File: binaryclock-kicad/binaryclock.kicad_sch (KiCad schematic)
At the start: 19 parts, among them J1 Conn_01x03_Pin, J2 AVR-ISP-6, SW1 SW_Push, SW2 SW_Push, SW3 SW_Push, U1 ATmega48-20P, Y1 Crystal

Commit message: assigned footprints to components
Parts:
- BT1: footprint (none) -> Battery:BatteryHolder_Keystone_103_1x20mm
- D1, D10, D11, D2, D3, D4, D5, D6, D7, D8, D9: footprint (none) -> LED_THT:LED_D3.0mm
- J1: footprint Connector_PinHeader_1.27mm:PinHeader_1x03_P1.27mm_Vertical -> Connector_PinHeader_2.54mm:PinHeader_1x03_P2.54mm_Vertical
- SW1, SW2, SW3: footprint (none) -> Button_Switch_THT:SW_PUSH_6mm
- Y1: footprint Crystal:Crystal_DS10_D1.0mm_L4.3mm_Vertical -> Crystal:Crystal_Round_D2.0mm_Vertical
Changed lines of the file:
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@@
 			)
 		)
-		(property "Footprint" ""
+		(property "Footprint" "LED_THT:LED_D3.0mm"
 			(at 140.97 76.2 0)
 			(effects
@@
 			)
 		)
-		(property "Footprint" "Connector_PinHeader_1.27mm:PinHeader_1x03_P1.27mm_Vertical"
+		(property "Footprint" "Connector_PinHeader_2.54mm:PinHeader_1x03_P2.54mm_Vertical"
 			(at 196.85 107.95 0)
 			(effects
@@
 			)
 		)
-		(property "Footprint" ""
+		(property "Footprint" "LED_THT:LED_D3.0mm"
 			(at 123.19 76.2 0)
 			(effects
@@
 			)
 		)
-		(property "Footprint" ""
+		(property "Footprint" "LED_THT:LED_D3.0mm"
 			(at 203.2 76.2 0)
 			(effects
@@
 			)
 		)
-		(property "Footprint" ""
+		(property "Footprint" "Button_Switch_THT:SW_PUSH_6mm"
 			(at 140.97 144.78 0)
 			(effects
@@
 			)
 		)
-		(property "Footprint" ""
+		(property "Footprint" "LED_THT:LED_D3.0mm"
 			(at 176.53 76.2 0)
 			(effects
@@
 			)
 		)
-		(property "Footprint" ""
+		(property "Footprint" "LED_THT:LED_D3.0mm"
 			(at 158.75 76.2 0)
 			(effects
@@
 			)
 		)
-		(property "Footprint" ""
+		(property "Footprint" "Button_Switch_THT:SW_PUSH_6mm"
 			(at 158.75 144.78 0)
 			(effects
@@
 			)
 		)
-		(property "Footprint" "Crystal:Crystal_DS10_D1.0mm_L4.3mm_Vertical"
+		(property "Footprint" "Crystal:Crystal_Round_D2.0mm_Vertical"
 			(at 138.43 110.49 0)
 			(effects
@@
 			)
 		)
-		(property "Footprint" ""
+		(property "Footprint" "Button_Switch_THT:SW_PUSH_6mm"
 			(at 125.73 144.78 0)
 			(effects
@@
 			)
 		)
-		(property "Footprint" ""
+		(property "Footprint" "LED_THT:LED_D3.0mm"
 			(at 149.86 76.2 0)
 			(effects
@@
 			)
 		)
-		(property "Footprint" ""
+		(property "Footprint" "Battery:BatteryHolder_Keystone_103_1x20mm"
 			(at 214.63 145.796 90)
 			(effects
@@
 			)
 		)
-		(property "Footprint" ""
+		(property "Footprint" "LED_THT:LED_D3.0mm"
 			(at 194.31 76.2 0)
 			(effects
@@
 			)
 		)
-		(property "Footprint" ""
+		(property "Footprint" "LED_THT:LED_D3.0mm"
 			(at 213.36 76.2 0)
 			(effects
@@
 			)
 		)
-		(property "Footprint" ""
+		(property "Footprint" "LED_THT:LED_D3.0mm"
 			(at 185.42 76.2 0)
 			(effects
@@
 			)
 		)
-		(property "Footprint" ""
+		(property "Footprint" "LED_THT:LED_D3.0mm"
 			(at 132.08 76.2 0)
 			(effects
@@
 			)
 		)
-		(property "Footprint" ""
+		(property "Footprint" "LED_THT:LED_D3.0mm"
 			(at 167.64 76.2 0)
 			(effects

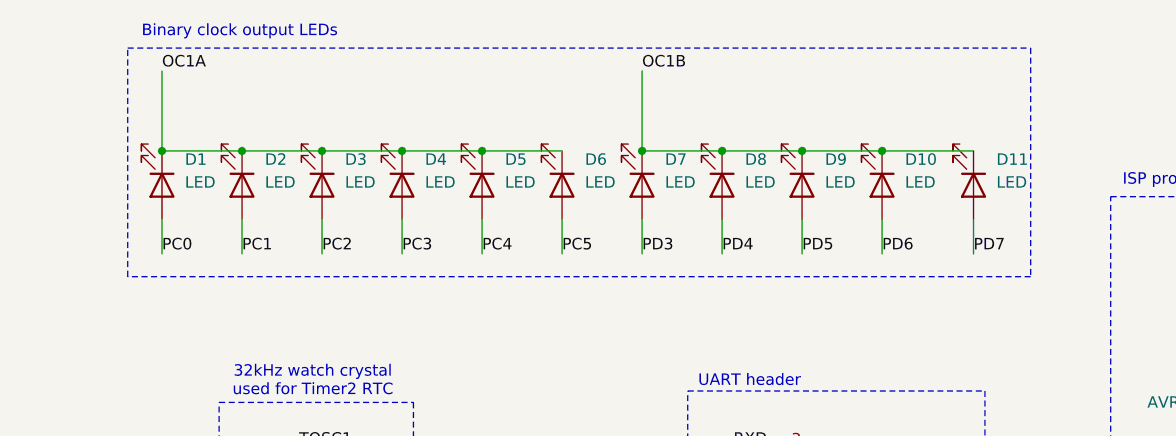
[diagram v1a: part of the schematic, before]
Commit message: passed drc
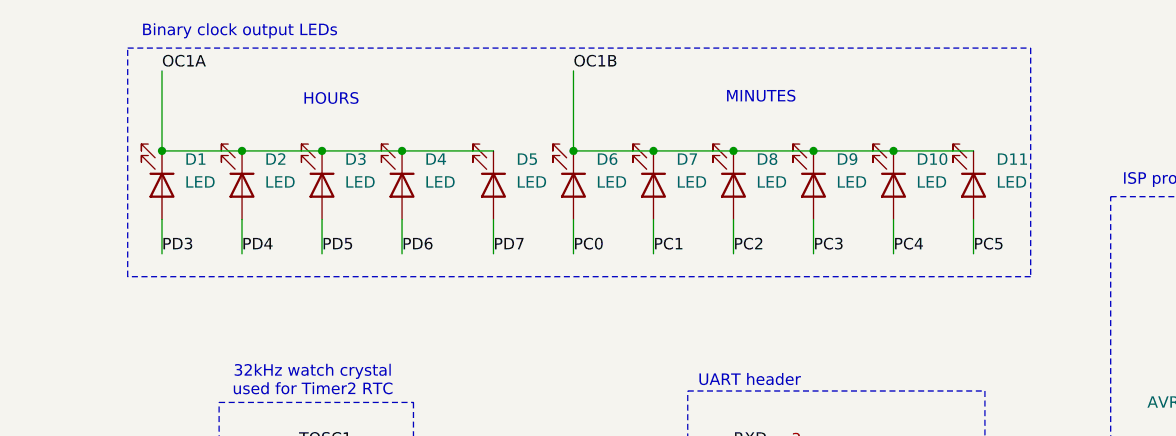
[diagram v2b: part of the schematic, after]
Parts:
- renumbered D7 to D1, D5 to D10, D6 to D11, D8 to D2, D9 to D3, D10 to D4, D11 to D5, D1 to D6, D2 to D7, D3 to D8, D4 to D9
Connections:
- net OC1A: now also D1.1 (K), D2.1 (K), D3.1 (K), D4.1 (K), D5.1 (K); no longer D10.1 (K), D11.1 (K), D6.1 (K), D7.1 (K), D8.1 (K), D9.1 (K)
- net OC1B: now also D10.1 (K), D11.1 (K), D6.1 (K), D7.1 (K), D8.1 (K), D9.1 (K); no longer D1.1 (K), D2.1 (K), D3.1 (K), D4.1 (K), D5.1 (K)
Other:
- note added: "HOURS"
- note added: "MINUTES"
- moved on the sheet: D1, D10, D11, D2, D3, D4, D5, D6, D7, D8, D9

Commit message: TRUE FINAL PCB VERSION
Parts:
- Y1: footprint Crystal:Crystal_Round_D2.0mm_Vertical -> Connector_PinHeader_2.54mm:PinHeader_1x02_P2.54mm_Vertical
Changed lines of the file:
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@@
 			)
 		)
-		(property "Footprint" "Crystal:Crystal_Round_D2.0mm_Vertical"
+		(property "Footprint" "Connector_PinHeader_2.54mm:PinHeader_1x02_P2.54mm_Vertical"
 			(at 138.43 110.49 0)
 			(effects
